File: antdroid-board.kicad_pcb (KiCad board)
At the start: 2 copper layers, 99.4 x 53.7 mm, 58 parts, among them P1 CONN_01X01, P2 CONN_01X01, Q1 BSS138, Q2 BSS138, U1 LM2678T-5.0, U2 LM2678T-5.0, U3 LM2675M-5

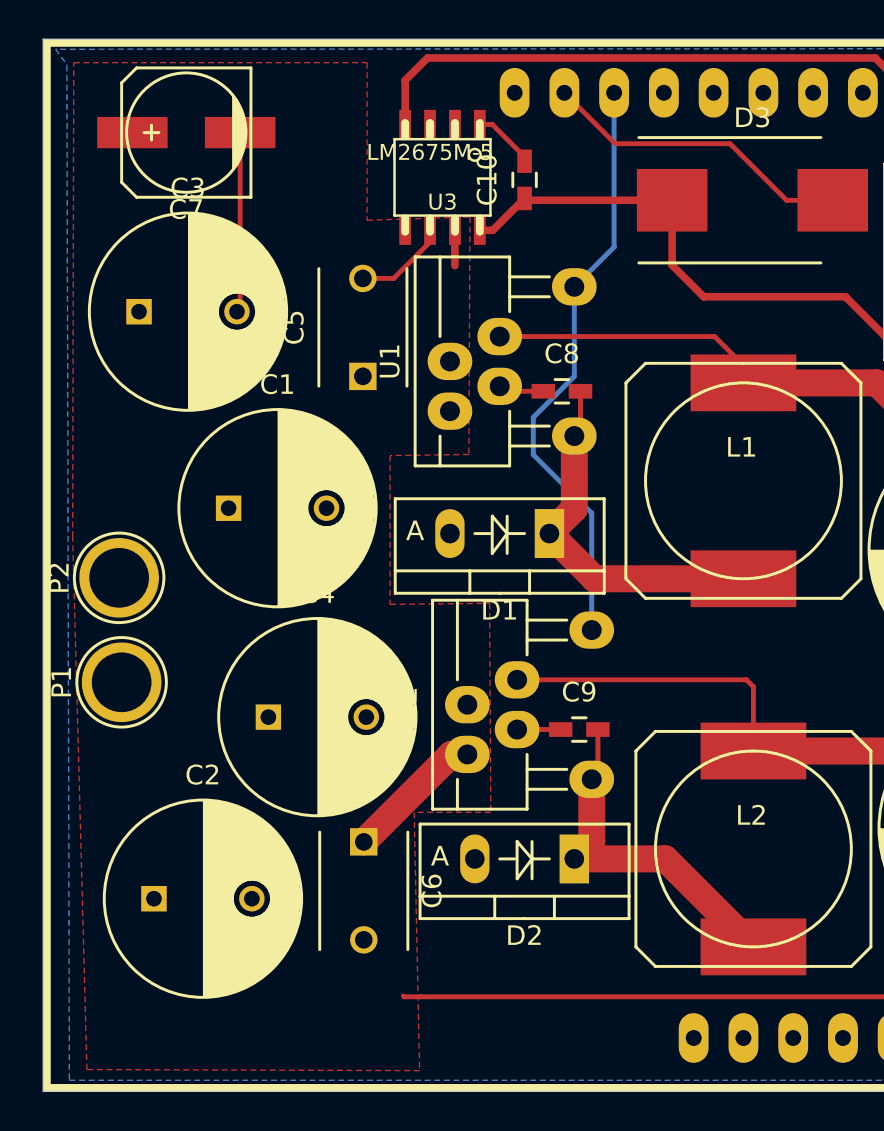
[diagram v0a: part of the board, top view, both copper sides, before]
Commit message: Added separation for heatsinks and outputs
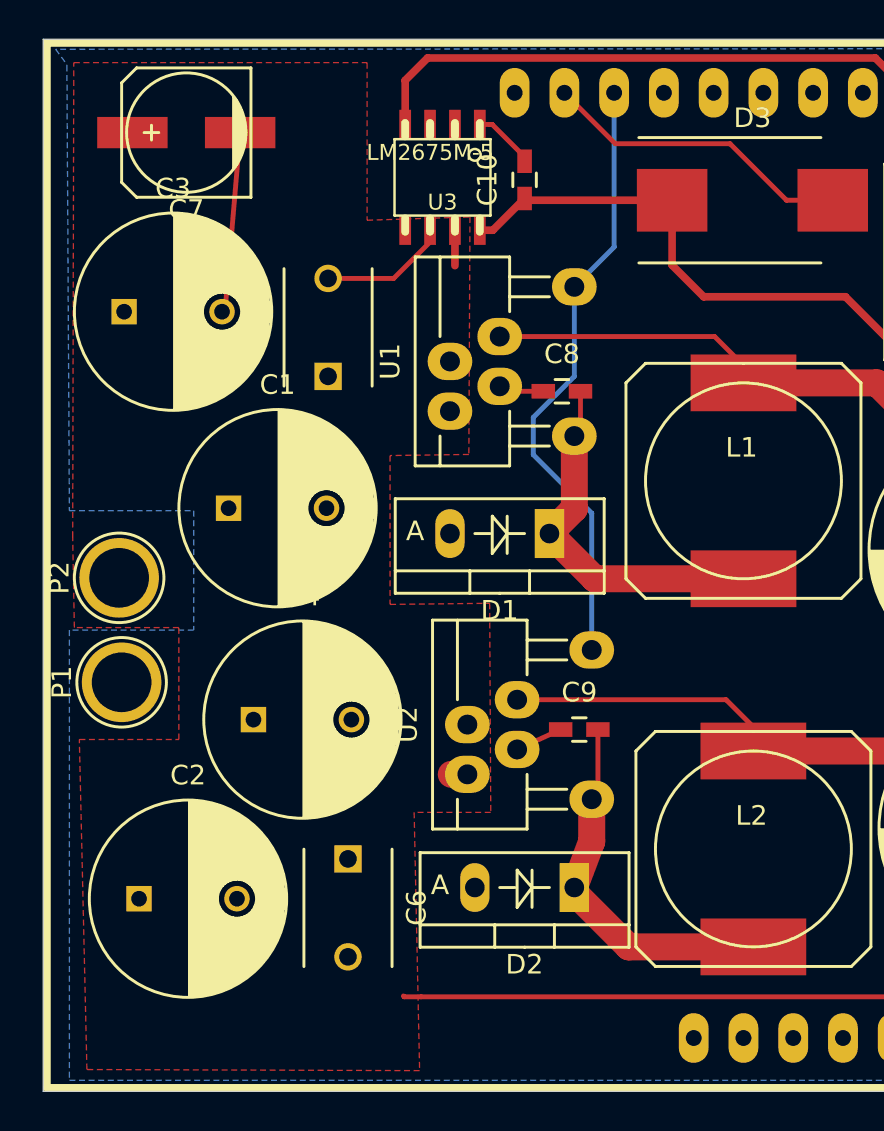
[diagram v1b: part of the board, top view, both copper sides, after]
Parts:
- moved C5 1.78 mm to (113.8, 90.2)
- moved D2 1.46 mm to (126.4, 116.3)
- moved C6 1.19 mm to (114.8, 114.8)
- moved U2 1.02 mm to (122.2, 108.0)
- moved C4 0.77 mm to (110.0, 107.7)
- moved C2 0.76 mm to (104.1, 116.8)
- moved C3 0.76 mm to (103.4, 86.9)
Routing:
- net VCC: track 41.7 -> 35.4 mm
- net GND: track 53.7 -> 55.5 mm
- net +5VD: track 71.6 -> 69.9 mm
- net /SERVO_ON: track 30.4 -> 31.4 mm
- net Net-(C9-Pad2): track 18.1 -> 18.9 mm

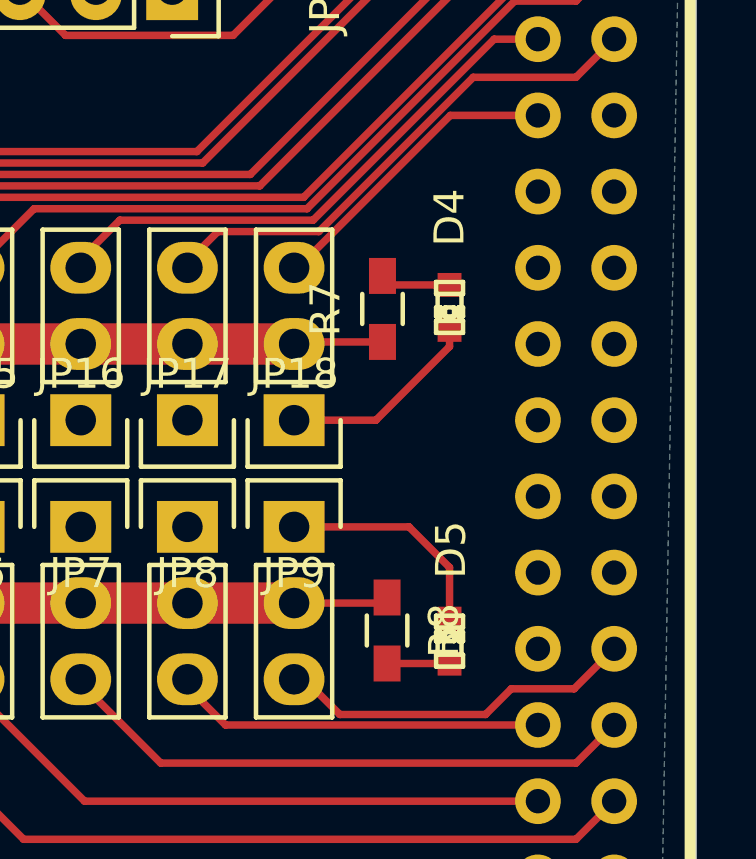
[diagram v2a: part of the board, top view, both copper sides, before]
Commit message: Added LED smd
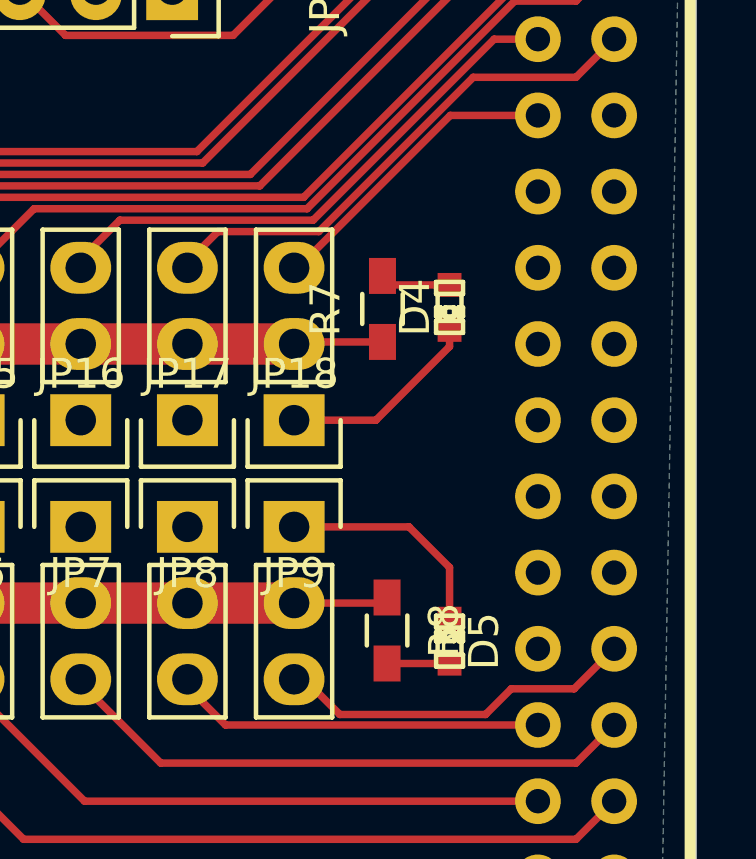
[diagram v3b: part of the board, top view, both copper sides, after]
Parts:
- C1, C2: value 2x470µF/25V -> 470µF/25V
- C8, C9: value 0,01µF -> 10nF
- D4, D5: footprint LEDs:LED-0603 -> antdroid-board:LED-0603
- R7, R8: value R -> 150Ω
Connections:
- D3 pad 1: Net-(C10-Pad1) -> GND
- D3 pad 2: GND -> Net-(C10-Pad1)
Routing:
- net Net-(C10-Pad1): track 32.7 -> 33.5 mm
- net GND: track 55.5 -> 54.7 mm

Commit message: Update some resistors
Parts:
- R1: value 30.1K -> 31.2K
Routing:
- net GND: track 54.7 -> 70.6 mm
- net Net-(C10-Pad1): track 33.5 -> 17.7 mm
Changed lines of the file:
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@@
       (effects (font (size 1 1) (thickness 0.15)))
     )
-    (fp_text value 30.1K (at 0 1.9) (layer F.Fab)
+    (fp_text value 31.2K (at 0 1.9) (layer F.Fab)
       (effects (font (size 1 1) (thickness 0.15)))
     )
@@
   (segment (start 131.3582 81.1784) (end 131.3582 84.4952) (width 0.391) (layer F.Cu) (net 2))
   (segment (start 131.3582 84.4952) (end 132.969 86.106) (width 0.391) (layer F.Cu) (net 2))
+  (segment (start 137.20064 81.1784) (end 134.3152 78.29296) (width 0.25) (layer F.Cu) (net 2))
+  (segment (start 132.969 86.106) (end 140.208 86.106) (width 0.391) (layer F.Cu) (net 2))
+  (segment (start 140.208 86.106) (end 143.43126 89.32926) (width 0.391) (layer F.Cu) (net 2))
   (segment (start 124.78 90.932) (end 122.809 90.932) (width 0.25) (layer F.Cu) (net 3))
   (segment (start 122.809 90.932) (end 122.555 90.678) (width 0.25) (layer F.Cu) (net 3))
@@
   (segment (start 127.254 113.919) (end 126.365 116.2685) (width 1.38) (layer F.Cu) (net 6) (status 20))
   (segment (start 139.5582 81.1784) (end 137.20064 81.1784) (width 0.25) (layer F.Cu) (net 7))
-  (segment (start 137.20064 81.1784) (end 134.3152 78.29296) (width 0.25) (layer F.Cu) (net 7))
   (segment (start 121.539 82.71) (end 122.202 82.71) (width 0.391) (layer F.Cu) (net 7))
   (segment (start 122.202 82.71) (end 123.825 81.087) (width 0.391) (layer F.Cu) (net 7))
   (segment (start 143.43126 89.32926) (end 148.209 89.32926) (width 0.391) (layer F.Cu) (net 7))
-  (segment (start 140.208 86.106) (end 143.43126 89.32926) (width 0.391) (layer F.Cu) (net 7))
-  (segment (start 132.969 86.106) (end 140.208 86.106) (width 0.391) (layer F.Cu) (net 7))
   (segment (start 131.3582 81.1784) (end 123.9164 81.1784) (width 0.391) (layer F.Cu) (net 7))
   (segment (start 123.9164 81.1784) (end 123.825 81.087) (width 0.391) (layer F.Cu) (net 7))

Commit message: Added aux pin. Finished?
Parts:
- added JP21: PINHD-1X3_2.54, antdroid-board:Pin_Header_Straight_1x03, F.Cu at (188.8, 98.6)
- moved R7 7.06 mm to (189.1, 101.9), turned to 0 degrees
- moved D5 1.49 mm to (191.3, 104.6)
- moved D4 1.45 mm to (191.3, 96.0), turned to 270 degrees
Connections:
- D3 pad 1: GND -> Net-(C10-Pad1)
- D3 pad 2: Net-(C10-Pad1) -> GND
- SHIELD1 pad 34: Net-(SHIELD1-Pad34) -> /AUX
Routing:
- net GND: track 70.6 -> 52.0 mm
- net Net-(C10-Pad1): track 17.7 -> 32.7 mm
- net +5VA: track 70.0 -> 77.0 mm
- net /AUX: track 0.00 -> 4.57 mm
- net Net-(D4-Pad2): track 2.36 -> 5.53 mm
- net Net-(D5-Pad2): track 2.08 -> 3.14 mm
- net VCC: track 35.4 -> 34.5 mm
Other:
- net class Power Rpi: trace_width 0.391 -> 0.6
- net class Servos +5V: trace_width 1.38 -> 1.6

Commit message: All revised, final release
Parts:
- added G***: ANTDROID-LOGO, antdroid-board:Antdroid-logo-8_5-8_5, F.Cu at (169.4, 116.6)
- moved G*** 16.8 mm to (181.1, 116.6)
- moved R3 3.36 mm to (161.0, 81.8), turned to 270 degrees
- moved C11 0.52 mm to (147.8, 96.0)
- moved JP20 0.51 mm to (181.7, 84.2)
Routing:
- net (no net): track 0.00 -> 31.6 mm
- net +5VP: track 55.5 -> 42.1 mm, vias 0 -> 2
- net +5V: track 71.3 -> 73.3 mm
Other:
- board text removed: "Antdroid board r1.0.0"

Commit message: Final release. Updated README Added board name in bottom silkscreen
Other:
- board text added: "Antdroid board r1"
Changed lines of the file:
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@@
     (area 91.14203 67.618 198.891501 126.942)
     (thickness 1.6)
-    (drawings 5)
+    (drawings 6)
     (tracks 275)
     (zones 0)
@@
     (visible_elements FFFFFFFF)
     (pcbplotparams
-      (layerselection 0x000e8_80000001)
+      (layerselection 0x000f8_80000001)
       (usegerberextensions true)
       (excludeedgelayer false)
@@
       (xy 3.473153 -3.071929) (xy 3.527958 -2.998955) (xy 3.527958 -2.998955)) (layer F.SilkS) (width 0.1))
   )
+  (gr_text "Antdroid board\nr1" (at 189.738 116.713) (layer B.SilkS)
+    (effects (font (size 2.5 2.5) (thickness 0.3)) (justify left mirror))
+  )
   (gr_line (start 99.24796 126.67488) (end 198.69404 126.67488) (angle 90) (layer Edge.Cuts) (width 0.01))

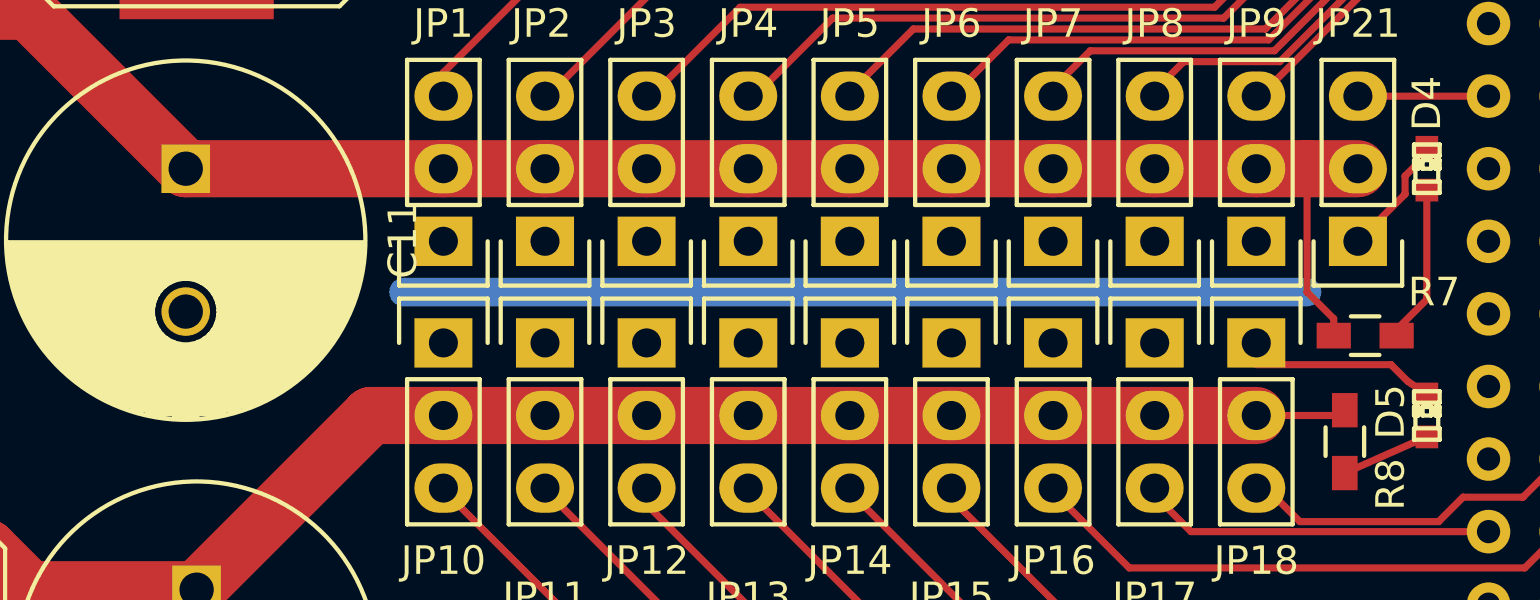
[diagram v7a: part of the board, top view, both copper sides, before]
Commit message: Fixed bottom gnd track
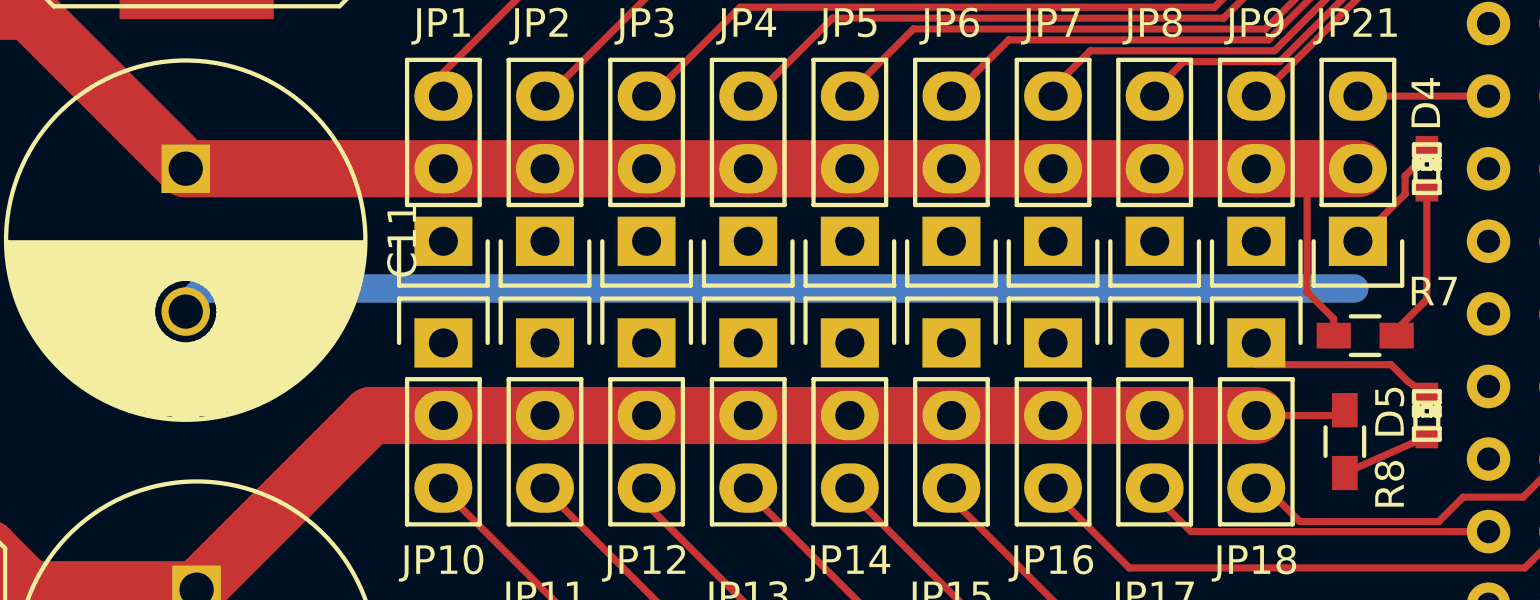
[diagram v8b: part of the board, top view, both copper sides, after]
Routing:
- net GND: track 52.0 -> 93.3 mm
- net (no net): track 31.6 -> 0.00 mm
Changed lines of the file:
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@@
     (thickness 1.6)
     (drawings 6)
-    (tracks 275)
+    (tracks 277)
     (zones 0)
     (modules 60)
@@
   )
   (layers
-    (0 F.Cu mixed)
+    (0 F.Cu mixed hide)
     (31 B.Cu power)
     (32 B.Adhes user)
@@
   )
   (setup
-    (last_trace_width 0.25)
+    (last_trace_width 1)
     (user_trace_width 0.25)
     (user_trace_width 0.6)
@@
   (gr_line (start 198.69404 74.35596) (end 197.29704 72.95896) (angle 90) (layer Edge.Cuts) (width 0.01))
   (gr_line (start 198.69404 126.67488) (end 198.69404 74.35596) (angle 90) (layer Edge.Cuts) (width 0.01))
-  (segment (start 187.071 100.33) (end 155.448 100.33) (width 1) (layer B.Cu) (net 0))
   (segment (start 120.269 82.71) (end 120.269 84.5185) (width 0.391) (layer F.Cu) (net 1))
   (segment (start 118.54688 121.84888) (end 117.6782 121.84888) (width 0.25) (layer F.Cu) (net 1))
@@
   (segment (start 145.161 123.952) (end 145.161 122.6996) (width 0.25) (layer F.Cu) (net 1))
   (segment (start 145.161 122.6996) (end 146.8042 121.0564) (width 0.25) (layer F.Cu) (net 1))
+  (segment (start 148.463 100.203) (end 188.722 100.203) (width 1) (layer B.Cu) (net 2))
+  (segment (start 147.828 100.838) (end 148.463 100.203) (width 1) (layer B.Cu) (net 2))
+  (segment (start 147.828 101.012) (end 147.828 100.838) (width 1) (layer B.Cu) (net 2))
   (segment (start 191.262 95.2627) (end 191.262 95.504) (width 0.25) (layer F.Cu) (net 2))
   (segment (start 191.262 95.504) (end 190.5 96.266) (width 0.25) (layer F.Cu) (net 2))
